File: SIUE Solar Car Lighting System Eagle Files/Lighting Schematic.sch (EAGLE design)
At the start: 43 parts, among them IC1 74HC08N, IC2 74HC08N, IC3 74LS04N, IC4 NE555N, Q1 RFP30N06LE, Q2 RFP30N06LE, Q3 RFP30N06LE, Q4 RFP30N06LE, Q5 RFP30N06LE, Q6 RFP30N06LE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

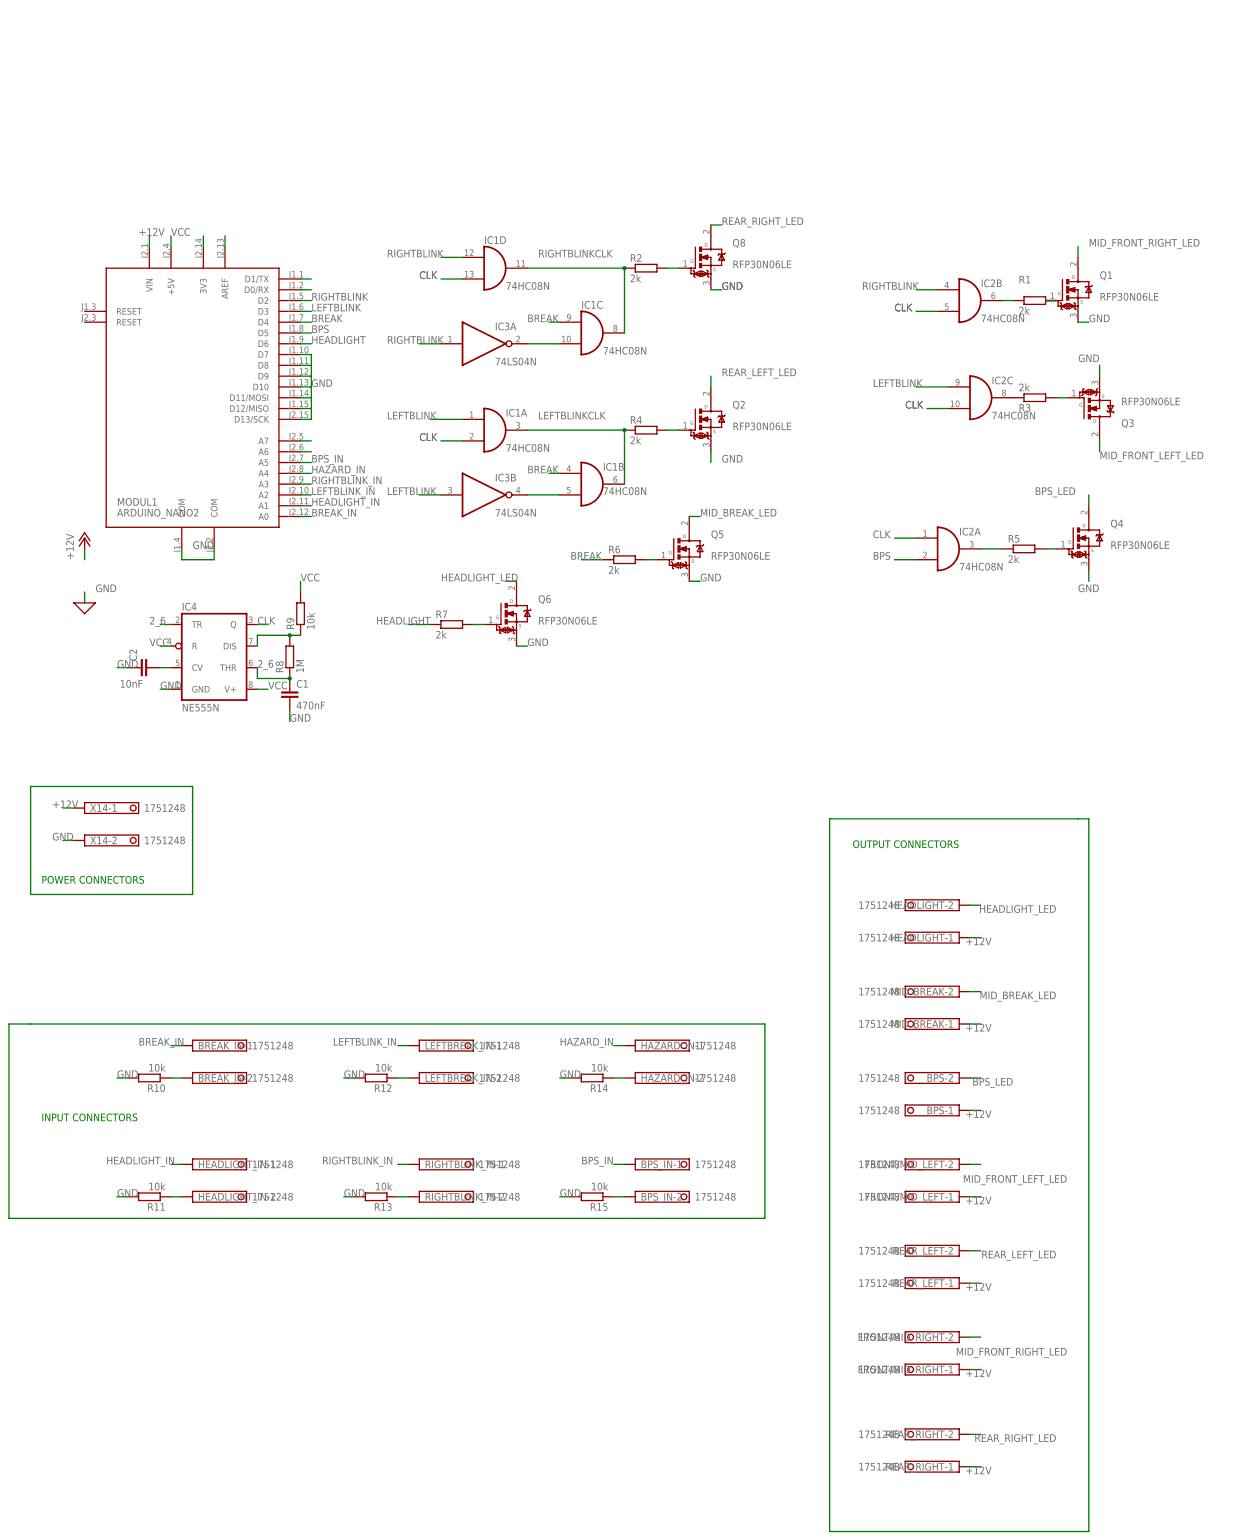
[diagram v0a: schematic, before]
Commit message: Add files via upload
Several changes made in this version:
- For the input connections I created an on-board 5V source on the positive end of the Input connector, and then a 10k pull-down resistor connected to the arduino on the other. This should make sure that the arduino isn't reading any floating signals when the switch is open and the 5V can not flow through the switch. The 5V source on the pins will also eliminate the need for an external power supply running across the switches. 
- This 5V source is included on the BPS_IN connector to allow for testing, in practical use since the BMS will be sending an HIGH Output when functioning correctly and go LOW when error is detected we should only need to plug in to the BPS IN-2 pin which has the pull-down resistor connected to it.
- I found that I was flawed in thinking I could set two logic gates entering the same node, which likely resulted in the issues I found when I first made the PCB board and will now be corrected with the addition of a single 74HC32 Quad 2-input OR chip. The new EAGLE Files and the LTSpice files reflect this change.
- I found that the holes I had originally placed where too small so I changed from 4 of those tiny holes to 3 - 3.2mm mounting holes placed at roughly 3 corners of the PCB to allow for mounting. 
-Minor movements in the EAGLE schematic or Board files to allow for easier soldering and less crowding.
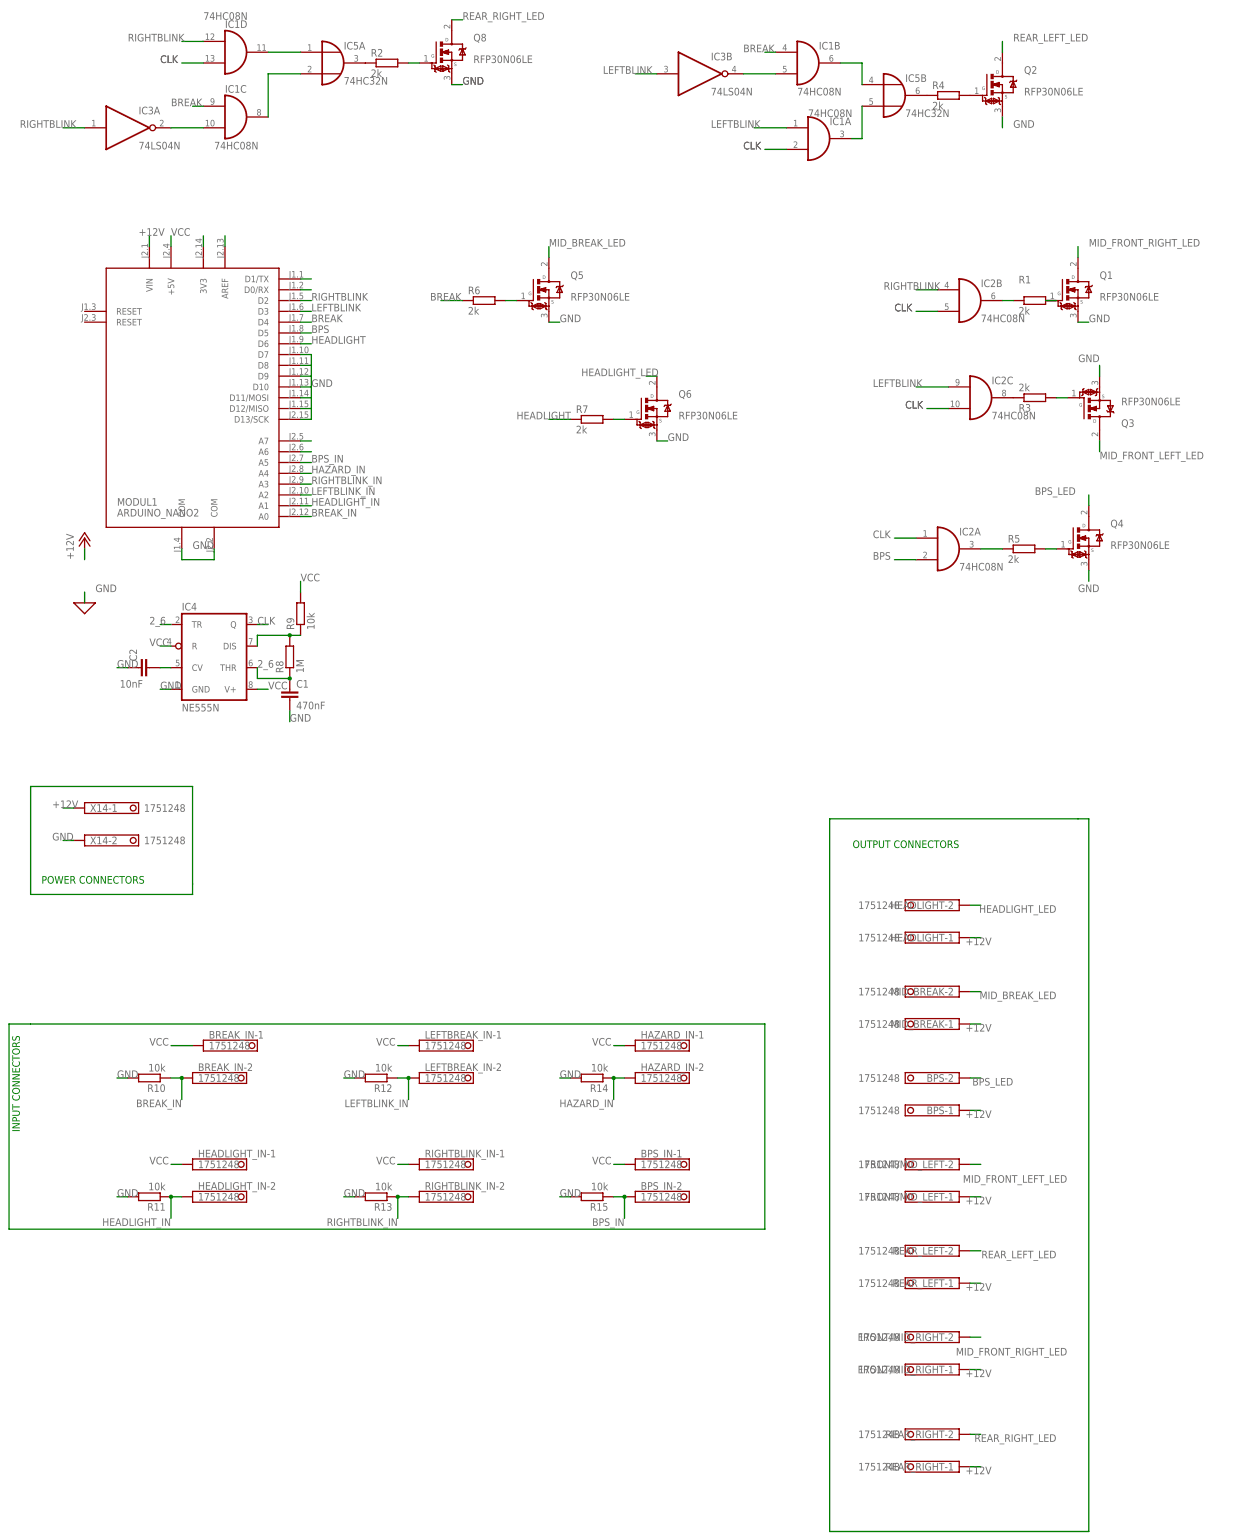
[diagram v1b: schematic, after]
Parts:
- added IC5: 74HC32N, 74xx-eu:74HC32N
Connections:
- removed net LEFTBLINKCLK: IC1A.O, IC1B.O, R4.1
- removed net N$46: BREAK_IN-2.K, R10.1
- removed net N$48: HEADLIGHT_IN-2.K, R11.1
- removed net N$50: LEFTBREAK_IN-2.K, R12.1
- removed net N$54: R13.1, RIGHTBLINK_IN-2.K
- removed net N$56: HAZARD_IN-2.K, R14.1
- removed net N$58: BPS_IN-2.K, R15.1
- removed net RIGHTBLINKCLK: IC1C.O, IC1D.O, R2.1
- new net N$17: IC5A.O, R2.1
- new net N$18: IC1C.O, IC5A.I1
- new net N$19: IC1D.O, IC5A.I0
- new net N$20: IC5B.O, R4.1
- new net N$21: IC1B.O, IC5B.I0
- new net N$22: IC1A.O, IC5B.I1
- net BPS_IN: now also BPS_IN-2.K, R15.1; no longer BPS_IN-1.K
- net BREAK_IN: now also BREAK_IN-2.K, R10.1; no longer BREAK_IN-1.K
- net HAZARD_IN: now also HAZARD_IN-2.K, R14.1; no longer HAZARD_IN-1.K
- net HEADLIGHT_IN: now also HEADLIGHT_IN-2.K, R11.1; no longer HEADLIGHT_IN-1.K
- net LEFTBLINK_IN: now also LEFTBREAK_IN-2.K, R12.1; no longer LEFTBREAK_IN-1.K
- net RIGHTBLINK_IN: now also R13.1, RIGHTBLINK_IN-2.K; no longer RIGHTBLINK_IN-1.K
- net VCC: now also BPS_IN-1.K, BREAK_IN-1.K, HAZARD_IN-1.K, HEADLIGHT_IN-1.K, LEFTBREAK_IN-1.K, RIGHTBLINK_IN-1.K
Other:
- moved on the sheet: BREAK_IN-1, IC1A, IC1B, IC1C, IC1D, IC3A, IC3B, Q2, Q5, Q6, Q8, R2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
